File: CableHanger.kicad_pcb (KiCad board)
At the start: 2 copper layers, 295 x 295 mm, 1 part

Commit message: Release Candidate 1
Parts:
- removed Ref**: Val**, SloBloFP:SloBloLogo_123x150
- added ?: , , F.Cu at (317.0, 232.0)
- added ?: , , F.Cu at (253.0, 168.0)
- added ?: , , F.Cu at (317.0, 168.0)
- added ?: , , F.Cu at (253.0, 232.0)
- added SloBloLogo: Val**, SloBloLogo_230x280, F.Cu at (285.0, 200.0)
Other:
- outline, holes or cut-outs redrawn

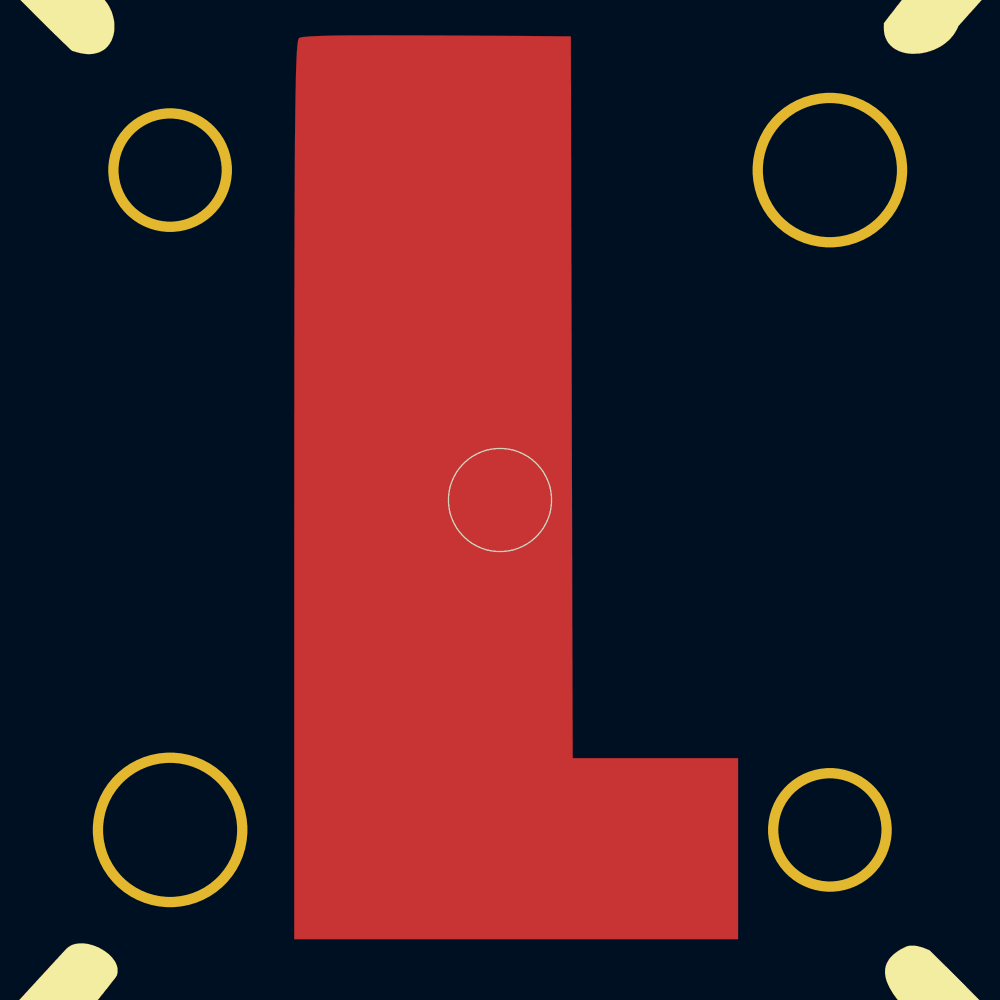
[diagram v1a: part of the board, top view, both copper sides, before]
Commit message: Add more toolholes
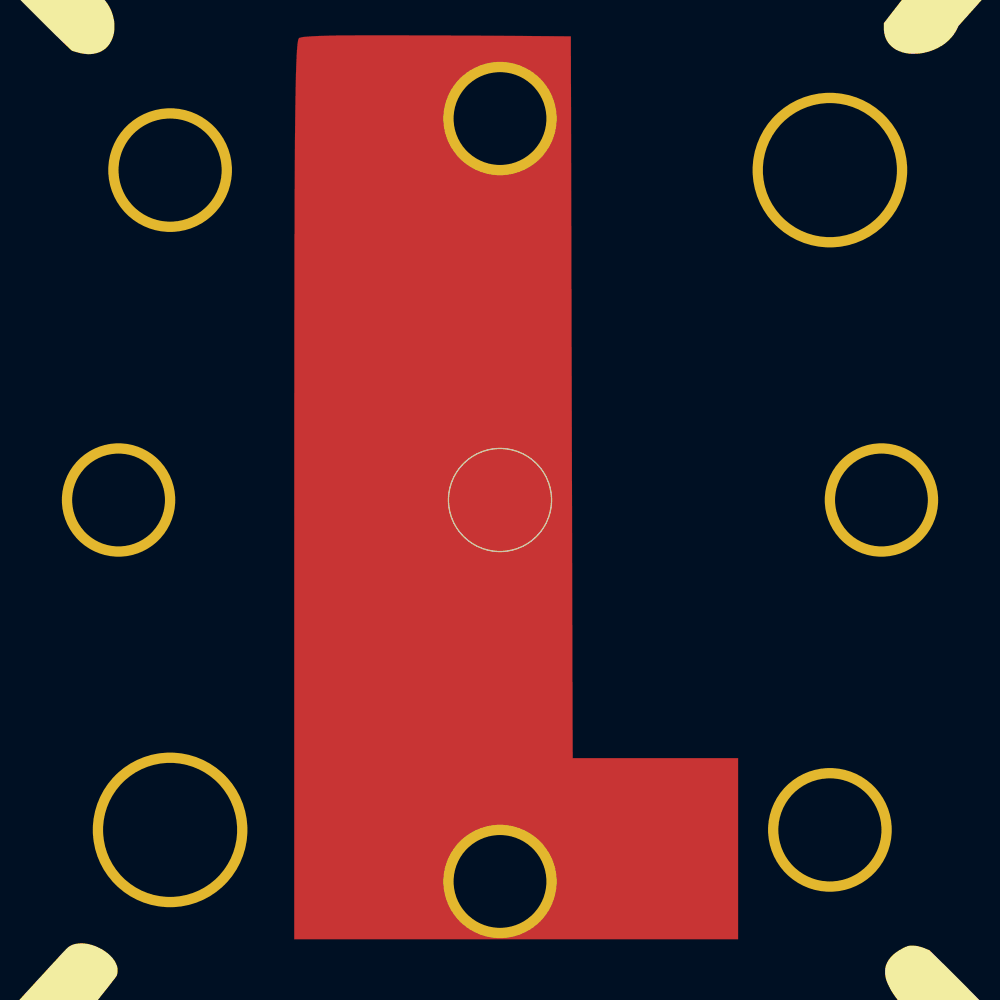
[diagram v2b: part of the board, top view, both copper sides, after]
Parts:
- added ?: , , F.Cu at (248.0, 200.0)
- added ?: , , F.Cu at (322.0, 200.0)
- added ?: , , F.Cu at (285.0, 163.0)
- added ?: , , F.Cu at (285.0, 237.0)
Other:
- board text added: "JLCJLCJLCJLC"
- board text added: "SloBlo Labs - Cable Hanger ${VERSION}"
